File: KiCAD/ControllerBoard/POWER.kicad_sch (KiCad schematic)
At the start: 13 parts, among them P2 CONN_POWER_FUSE, Q6 55V 31A 65mOhm, U12 TSR_1-24120, U13 TSR_1-2450, U14 TSR_1-2433

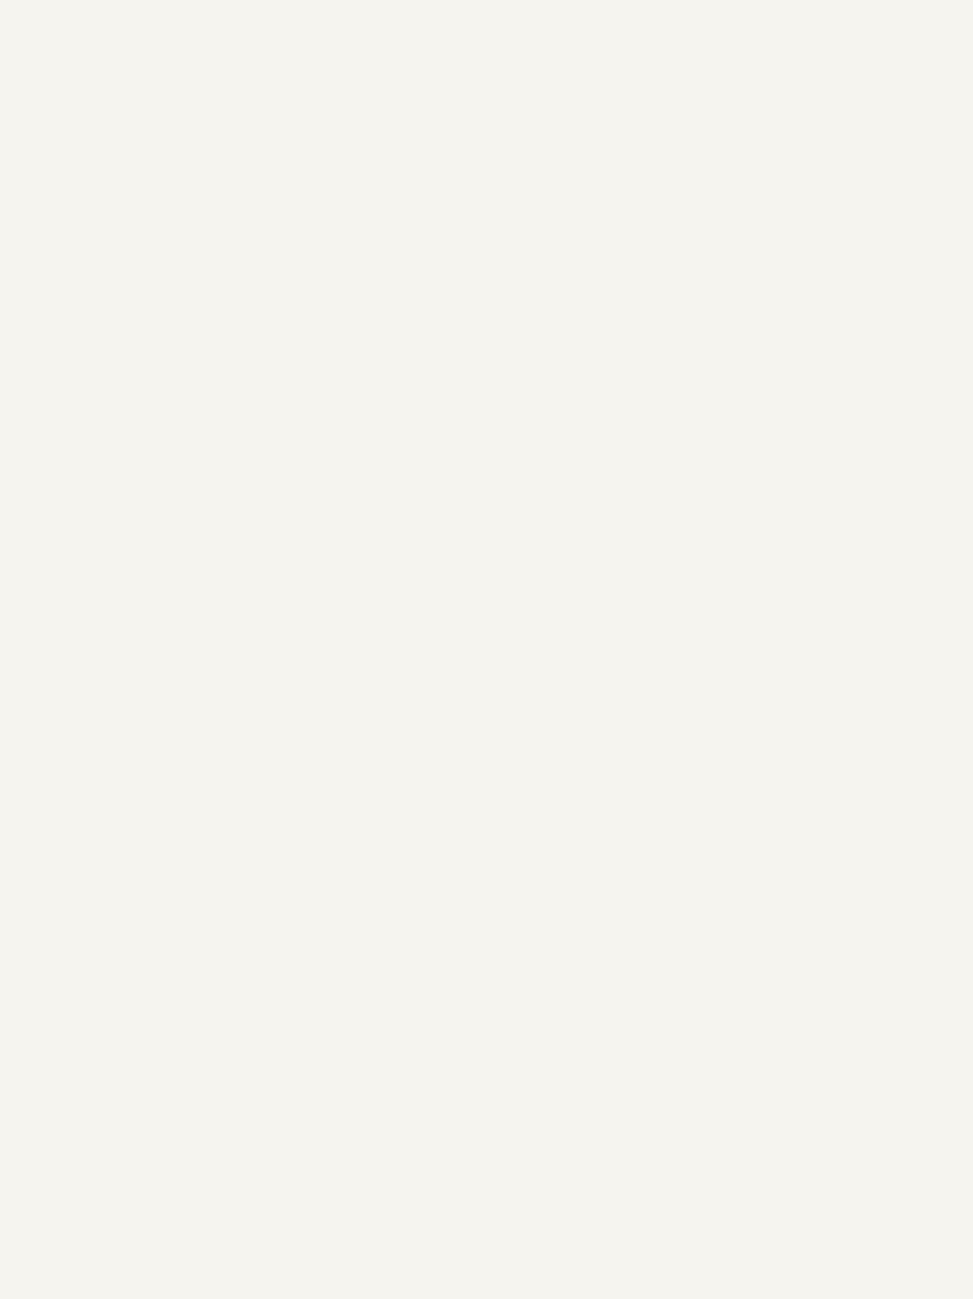
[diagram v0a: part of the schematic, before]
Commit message: CPU symbol changed, all pins on one page
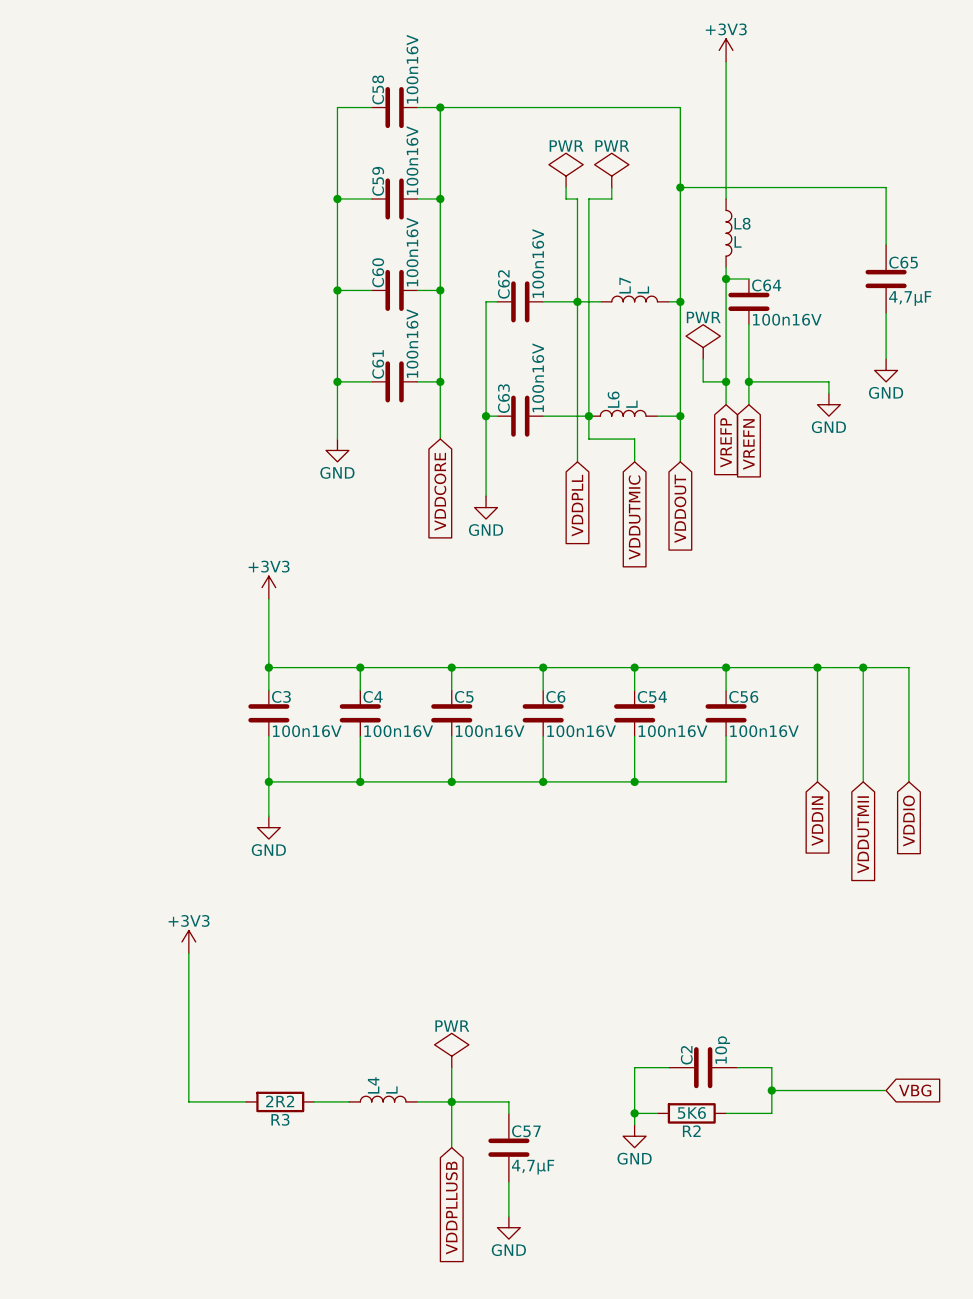
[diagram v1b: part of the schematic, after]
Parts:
- added C2: 10p, mylib:C_1206, symbol ATSAME70:C
- added C3, C4, C5, C54, C56, C58, C59, C6, C60, C61, C62, C63, C64: 100n16V, ATSAME70:C_0402, symbol ATSAME70:C_100n_16V_0402
- added C57, C65: 4,7µF, mylib:C_1206, symbol ATSAME70:C
- added L4: L, mylib:L_Chip_1210, symbol ATSAME70:L
- added L6, L7, L8: L, mylib:C_1207_Reflow, symbol ATSAME70:L
- added R2: 5K6, ATSAME70:R_0805, symbol ATSAME70:R_5K6_0603
- added R3: 2R2, mylib:R_1206, symbol ATSAME70:R
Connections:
- net GND: now also C2.1, C3.2, C4.2, C5.2, C54.2, C56.2, C57.2, C58.1, C59.1, C6.2, C60.1, C61.1, C62.1, C63.1, C64.2, C65.2, R2.2
- new net: L4.1, R3.1
- new net +3V3: C3.1, C4.1, C5.1, C54.1, C56.1, C6.1, L8.1, R3.2
- new net VBG: C2.2, R2.1
- new net VDDCORE: C58.2, C59.2, C60.2, C61.2, C65.1, L6.2, L7.2
- new net VDDPLL: C62.2, L7.1
- new net VDDPLLUSB: C57.1, L4.2
- new net VDDUTMIC: C63.2, L6.1
- new net VREFP: C64.1, L8.2
